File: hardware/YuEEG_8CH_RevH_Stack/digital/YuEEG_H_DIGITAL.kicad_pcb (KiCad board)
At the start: 6 copper layers, 48 x 60 mm, 116 parts, among them J1101 KINGCONN 7TFCN-FA-1010-C / H3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, J2002 OK-14F024-04 / AM178Q368448LK, J301 DEBUG POGO / NO HEADER FITTED, J601 USB-C DATA / FLASH - ISOLATED, Q1001 MMBT3904 OE ENABLE, SW1001 ALPS SKRTLBE010 / REC, SW301 ALPS SKRTLBE010 / RESET, SW302 ALPS SKRTLBE010 / BOOT, U1001 TPS22918DBVR AMOLED POWER, U1003 TPS7A2018PDBVR, U1004 SN74AXC8T245PWR / 3V3 -> 1V8, U2 ESP32-S3-WROOM-1U-N16R8, U402 TPS62160DGKR, U701 ADuM4160BRIZ / enhanced creep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

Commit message: Refine Rev H module legends and USB return paths
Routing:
- net GND: vias 39 -> 41
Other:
- board text added: "3V3"
- board text added: "DISPLAY"
- board text added: "MCU / RF"
- board text added: "POWER"
- board text added: "SD"

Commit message: Improve host USB return paths and assess compact partition
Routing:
- net HOST_GND: vias 5 -> 7
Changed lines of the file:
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@@
+	)
+	(via
+		(at 27.85 49.4)
+		(size 0.45)
+		(drill 0.2)
+		(layers "F.Cu" "B.Cu")
+		(net 46)
 	)
 	(via
@@
 		(drill 0.2)
 		(layers "F.Cu" "B.Cu")
+		(net 46)
+	)
+	(via
+		(at 23.7 49.4)
+		(size 0.45)
+		(drill 0.2)
+		(layers "F.Cu" "B.Cu")

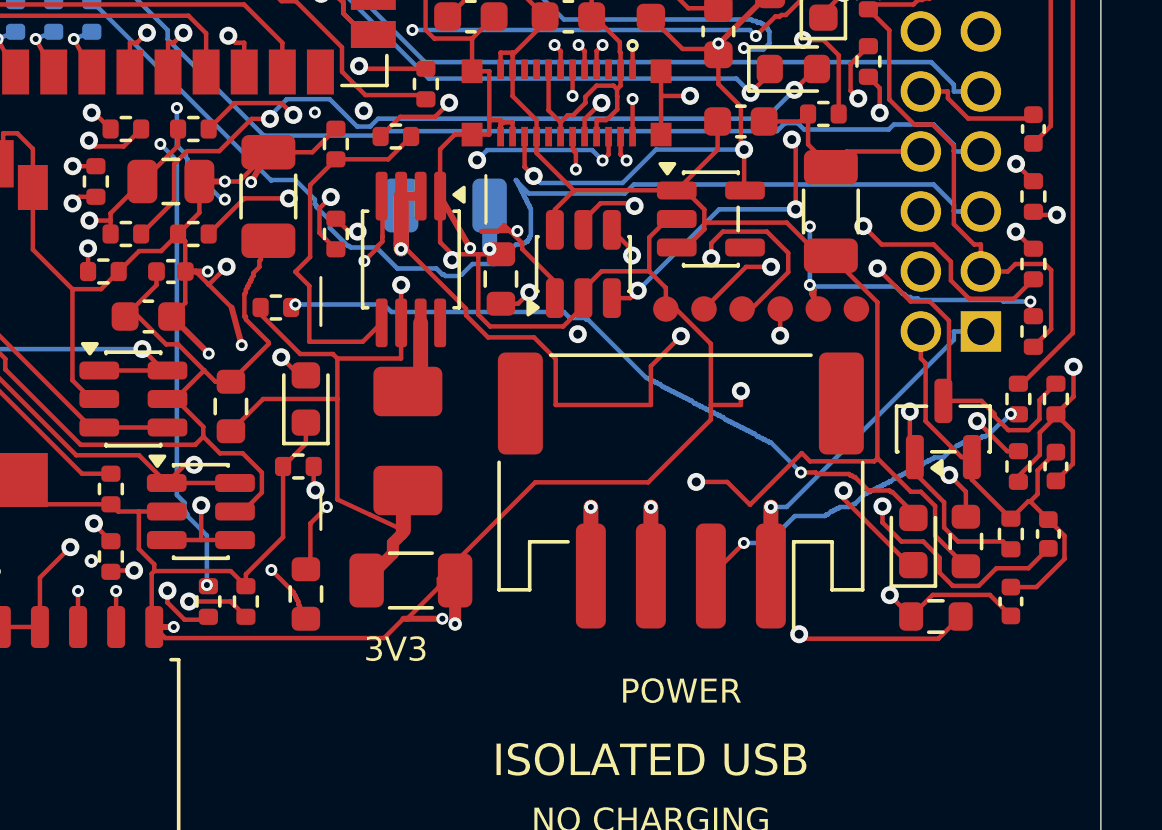
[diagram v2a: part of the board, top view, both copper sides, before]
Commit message: Route right-facing PH4 power entry and review stacked cable clearance
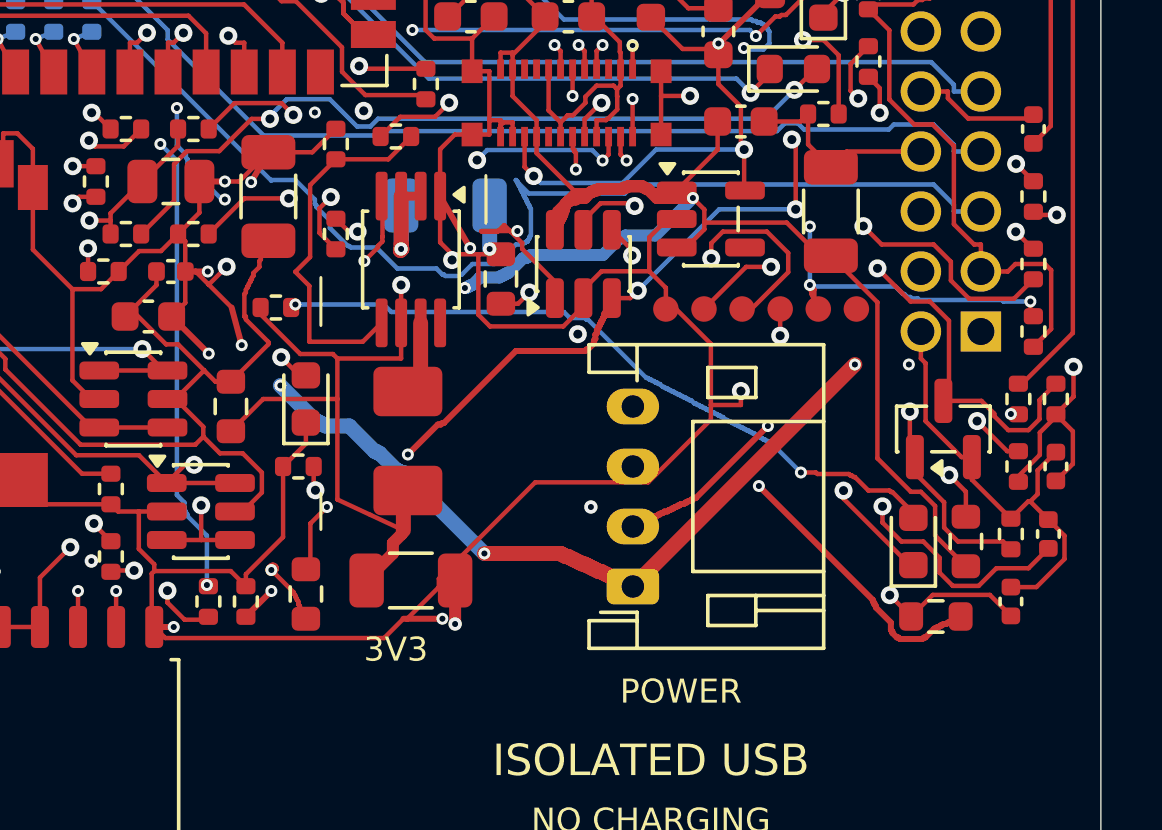
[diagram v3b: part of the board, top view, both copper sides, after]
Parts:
- JH2: value POWER INPUT: 1=5V 2=CELL_SENSE 3/4=GND -> S4B-PH-K-S / 5V+CELL SENSE / RIGHT; footprint Connector_JST:JST_PH_S4B-PH-SM4-TB_1x04-1MP_P2.00mm_Horizontal -> Connector_JST:JST_PH_S4B-PH-K_1x04_P2.00mm_Horizontal
- moved JH2 3.58 mm to (32.4, 38.5), turned to 90 degrees
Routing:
- net AM_POWER_EN: track 72.1 -> 54.2 mm, vias 6 -> 7
- net GND: track 354.7 -> 350.1 mm, vias 41 -> 40
- net AM_RAW: track 79.2 -> 83.4 mm, vias 3 -> 4
- net BAT_PROTECTED_SENSE: track 12.5 -> 14.7 mm
- net SYS_5V: track 62.2 -> 61.2 mm, vias 3 -> 5
- net VCI_EN: track 31.5 -> 32.0 mm

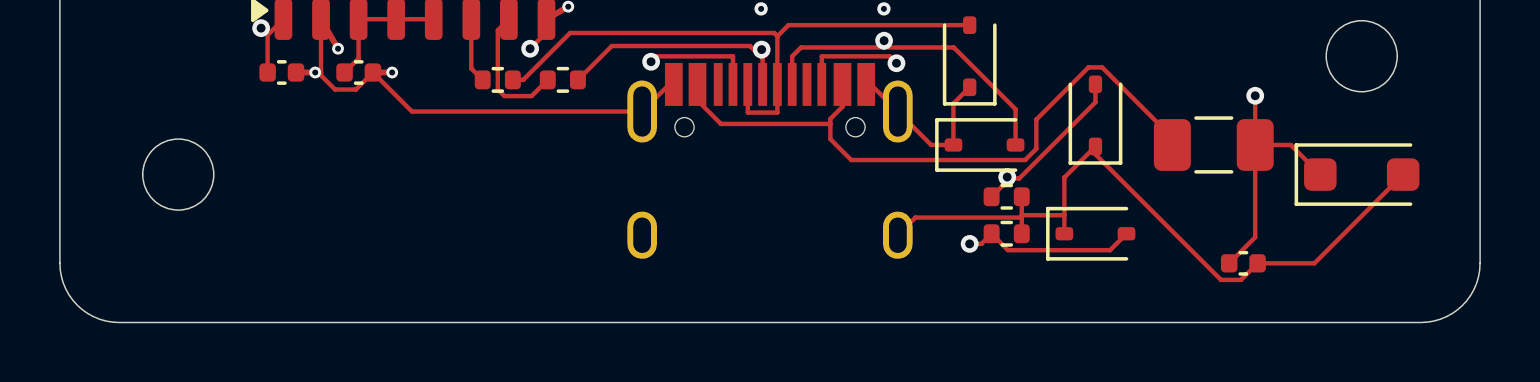
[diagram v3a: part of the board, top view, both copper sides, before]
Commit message: Refine stacked AFE clearance and rounded USB mouth geometry
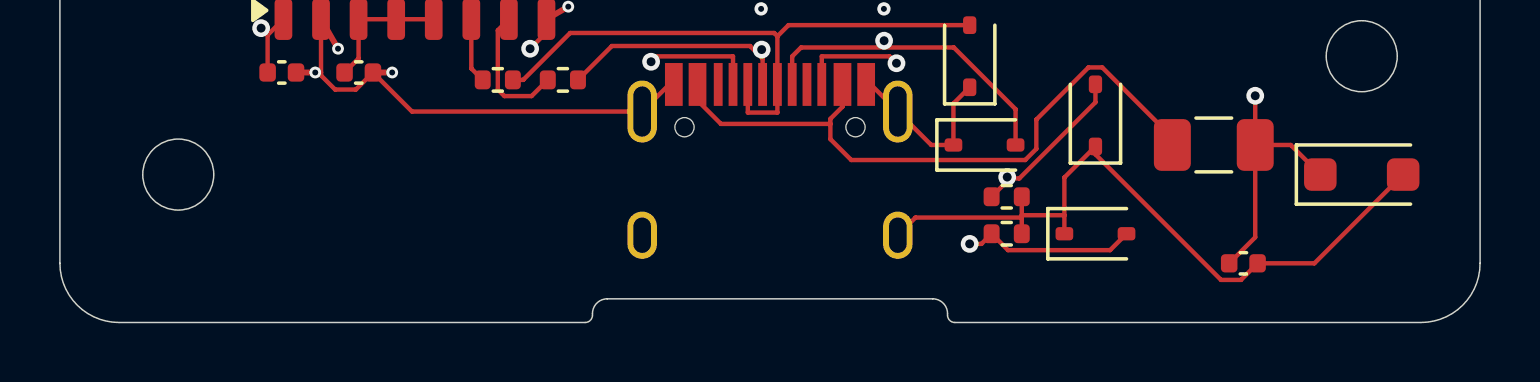
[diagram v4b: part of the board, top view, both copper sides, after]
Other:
- outline, holes or cut-outs redrawn
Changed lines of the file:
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@@
 no)
 (model
-"${KICAD9_3DMODEL_DIR}/Connector_USB.3dshapes/USB_C_Receptacle_HRO_TYPE-C-31-M-12.step"
+"${KIPRJMOD}/../models/HRO_TYPE_C_31_M_12_original_envelope.wrl"
 (offset
 (xyz
@@
 (uuid
 "45773c78-1e34-4620-b6f3-964a9d79a8df"))
+(gr_line
+(start
+29.5
+59.2)
+(end
+18.5
+59.2)
+(stroke
+(width
+0.05)
+(type
+default))
+(layer
+"Edge.Cuts")
+(uuid
+"472d506f-4891-4d32-b6f5-09d8172f2f48"))
+(gr_line
+(start
+30
+59.75)
+(end
+30
+59.7)
+(stroke
+(width
+0.05)
+(type
+default))
+(layer
+"Edge.Cuts")
+(uuid
+"518580e5-4c22-4891-a297-6132da3c291a"))
+(gr_line
+(start
+17.75
+60)
+(end
+2
+60)
+(stroke
+(width
+0.05)
+(type
+default))
+(layer
+"Edge.Cuts")
+(uuid
+"52b9dd57-f194-49a0-a3fb-2fe70832e1f6"))
 (gr_arc
 (start
@@
 (uuid
 "5b0a4cb1-9b67-4340-887e-302c1bf2965b"))
+(gr_arc
+(start
+30.25
+60)
+(mid
+30.073223
+59.926777)
+(end
+30
+59.75)
+(stroke
+(width
+0.05)
+(type
+default))
+(layer
+"Edge.Cuts")
+(uuid
+"5d0bf896-d021-4e8a-98c2-f4afe4b75afb"))
+(gr_line
+(start
+46
+60)
+(end
+30.25
+60)
+(stroke
+(width
+0.05)
+(type
+default))
+(layer
+"Edge.Cuts")
+(uuid
+"64c7cb2d-d89a-4fb0-9695-b3c973a9714f"))
 (gr_line
 (start
@@
 (gr_arc
 (start
+18
+59.7)
+(mid
+18.146447
+59.346447)
+(end
+18.5
+59.2)
+(stroke
+(width
+0.05)
+(type
+default))
+(layer
+"Edge.Cuts")
+(uuid
+"76488821-a534-423e-a743-6a43400ad53d"))
+(gr_arc
+(start
+29.5
+59.2)
+(mid
+29.853553
+59.346447)
+(end
+30
+59.7)
+(stroke
+(width
+0.05)
+(type
+default))
+(layer
+"Edge.Cuts")
+(uuid
+"863269dc-fa3c-40b6-9685-5c1e3fb14c25"))
+(gr_arc
+(start
 46
 0)
@@
 (gr_arc
 (start
+18
+59.75)
+(mid
+17.926777
+59.926777)
+(end
+17.75
+60)
+(stroke
+(width
+0.05)
+(type
+default))
+(layer
+"Edge.Cuts")
+(uuid
+"a8cc7517-05e0-434c-b6f1-4bfbc258521d"))
+(gr_arc
+(start
 2
 60)
@@
 (gr_line
 (start
-46
-60)
+18
+59.7)
 (end
-2
-60)
+18
+59.75)
 (stroke
 (width
@@
 "Edge.Cuts")
 (uuid
-"d7378dbb-97dc-4bd2-8657-7e1925d609d5"))
+"da61484d-36c7-46f5-9e3e-5574fb2db7a4"))
 (gr_text
 "MCU / RF"

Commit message: Constrain display clearance resistor height and audit remaining design gates
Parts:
- R1101: value 22R -> 22R 1% / RC0402FR-0722RL; footprint Resistor_SMD:R_0402_1005Metric -> YuEEG:YAGEO_RC0402FR_0722RL
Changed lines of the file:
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@@
 0))))
 (footprint
-"Resistor_SMD:R_0402_1005Metric"
+"YuEEG:YAGEO_RC0402FR_0722RL"
 (layer
 "F.Cu")
@@
 (property
 "Value"
-"22R"
+"22R 1% / RC0402FR-0722RL"
 (at
 0
@@
 (property
 "Datasheet"
-""
+"https://www.yageogroup.com/component-documentation/download/specsheet/RC0402FR-0722RL"
 (at
 0
@@
 no)
 (model
-"${KICAD9_3DMODEL_DIR}/Resistor_SMD.3dshapes/R_0402_1005Metric.step"
+"${KIPRJMOD}/../models/YAGEO_RC0402FR_0722RL_max_envelope.wrl"
 (offset
 (xyz
